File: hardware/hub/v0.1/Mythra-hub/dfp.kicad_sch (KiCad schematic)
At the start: 0 parts

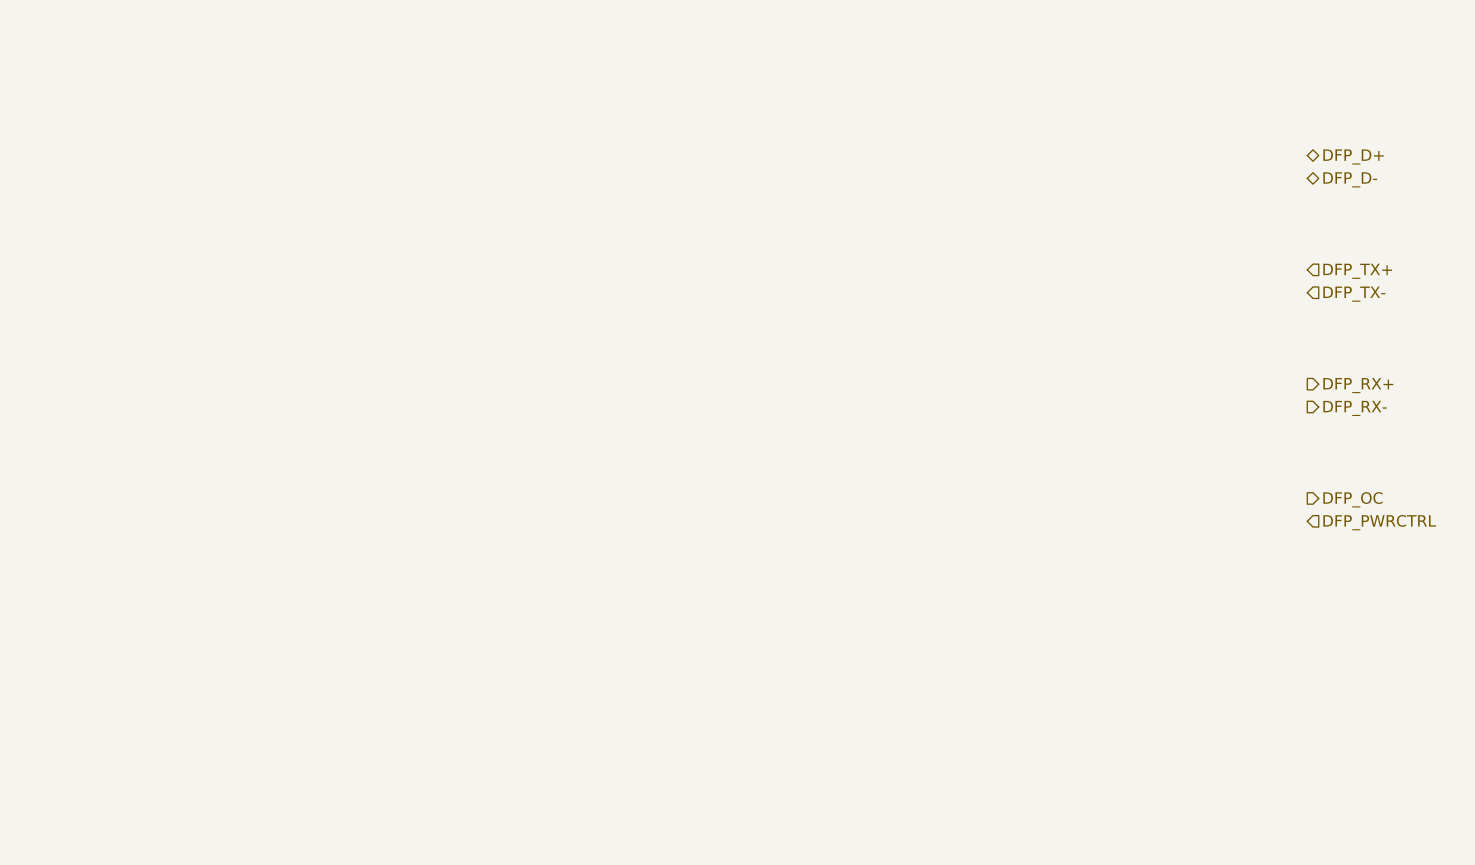
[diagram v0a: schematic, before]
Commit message: Created the DC-DC supply for the hub's core 1.1V rail and added the DFP Type-C recepticals and their shield components
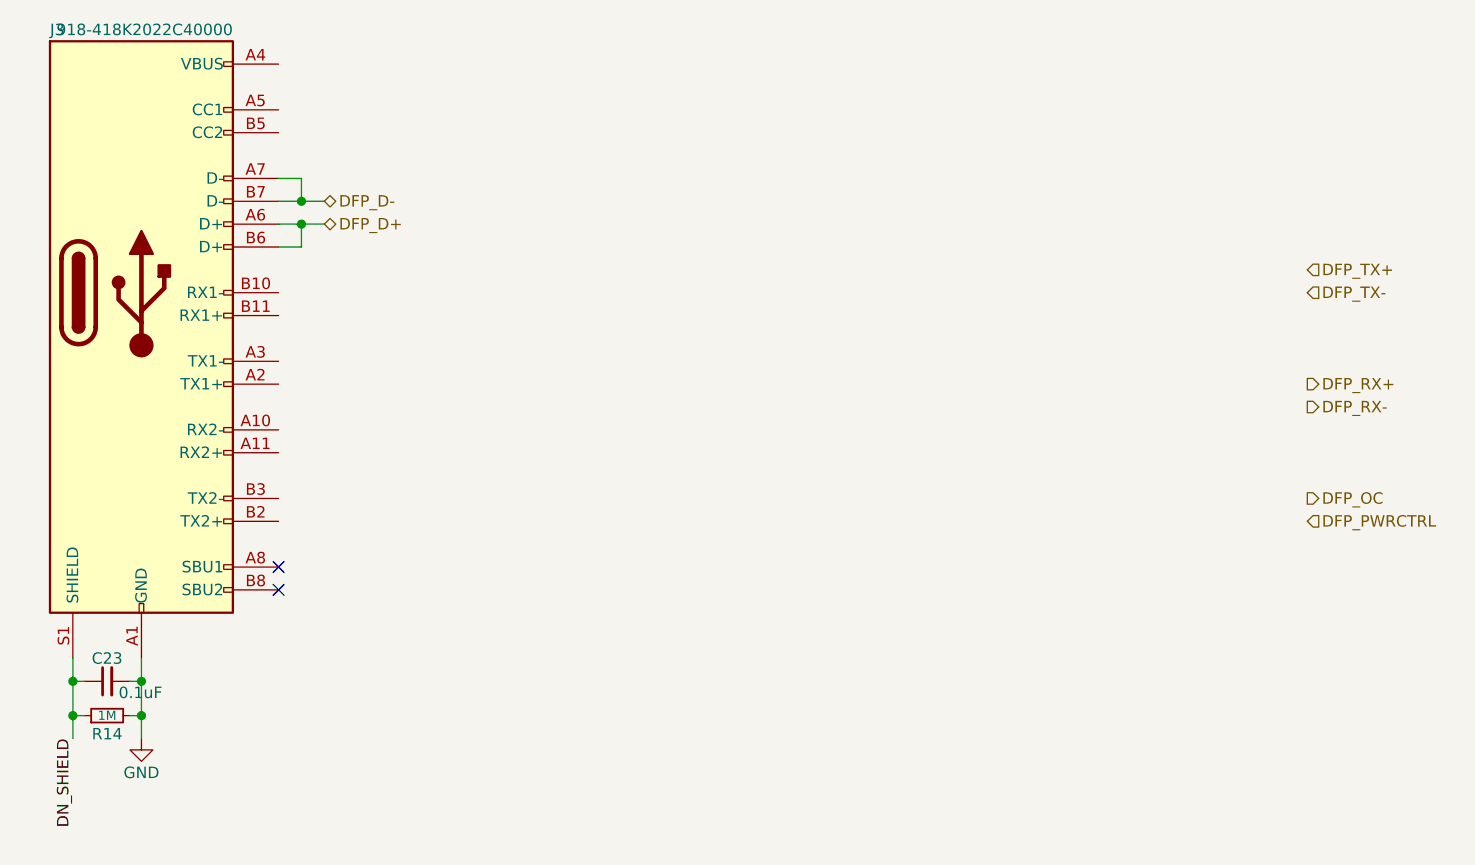
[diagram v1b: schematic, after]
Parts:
- added C23: 0.1uF, rhais_rcl:C0402, symbol Device:C_Small
- added J3: 918-418K2022C40000, rhais_usb:USB-3.1-Type-C_In-PCB, symbol Connector:USB_C_Receptacle
- added R14: 1M, rhais_rcl:R0402, symbol Device:R_Small
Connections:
- net DFP_D+: now also J3.A6 (D+), J3.B6 (D+)
- net DFP_D-: now also J3.A7 (D-), J3.B7 (D-)
- new net: J3.A4 (VBUS), J3.A9 (VBUS), J3.B4 (VBUS), J3.B9 (VBUS)
- new net DN_SHIELD: C23.1, J3.S1 (SHIELD), R14.1
- new net GND: C23.2, J3.A1 (GND), J3.A12 (GND), J3.B1 (GND), J3.B12 (GND), R14.2
- no-connect marks 0 -> 2
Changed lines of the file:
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@@
 (kicad_sch (version 20210621) (generator eeschema)
   (paper "A4")
-  (hierarchical_label "DFP_D+" (shape bidirectional) (at 165.1 88.9 0)
-    (effects (font (size 1.27 1.27)) (justify left))
-  )
-  (hierarchical_label "DFP_D-" (shape bidirectional) (at 165.1 91.44 0)
+  (junction (at 27.94 147.32) (diameter 1.016) (color 0 0 0 0))
+  (junction (at 27.94 151.13) (diameter 1.016) (color 0 0 0 0))
+  (junction (at 35.56 147.32) (diameter 1.016) (color 0 0 0 0))
+  (junction (at 35.56 151.13) (diameter 1.016) (color 0 0 0 0))
+  (junction (at 53.34 93.98) (diameter 1.016) (color 0 0 0 0))
+  (junction (at 53.34 96.52) (diameter 1.016) (color 0 0 0 0))
+  (no_connect (at 50.8 134.62))
+  (no_connect (at 50.8 137.16))
+  (wire (pts (xy 27.94 147.32) (xy 27.94 144.78))
+    (stroke (width 0) (type solid) (color 0 0 0 0))
+  )
+  (wire (pts (xy 27.94 151.13) (xy 27.94 147.32))
+    (stroke (width 0) (type solid) (color 0 0 0 0))
+  )
+  (wire (pts (xy 27.94 151.13) (xy 27.94 153.67))
+    (stroke (width 0) (type solid) (color 0 0 0 0))
+  )
+  (wire (pts (xy 29.21 147.32) (xy 27.94 147.32))
+    (stroke (width 0) (type solid) (color 0 0 0 0))
+  )
+  (wire (pts (xy 29.21 151.13) (xy 27.94 151.13))
+    (stroke (width 0) (type solid) (color 0 0 0 0))
+  )
+  (wire (pts (xy 34.29 147.32) (xy 35.56 147.32))
+    (stroke (width 0) (type solid) (color 0 0 0 0))
+  )
+  (wire (pts (xy 34.29 151.13) (xy 35.56 151.13))
+    (stroke (width 0) (type solid) (color 0 0 0 0))
+  )
+  (wire (pts (xy 35.56 147.32) (xy 35.56 144.78))
+    (stroke (width 0) (type solid) (color 0 0 0 0))
+  )
+  (wire (pts (xy 35.56 151.13) (xy 35.56 147.32))
+    (stroke (width 0) (type solid) (color 0 0 0 0))
+  )
+  (wire (pts (xy 35.56 153.67) (xy 35.56 151.13))
+    (stroke (width 0) (type solid) (color 0 0 0 0))
+  )
+  (wire (pts (xy 50.8 93.98) (xy 53.34 93.98))
+    (stroke (width 0) (type solid) (color 0 0 0 0))
+  )
+  (wire (pts (xy 50.8 96.52) (xy 53.34 96.52))
+    (stroke (width 0) (type solid) (color 0 0 0 0))
+  )
+  (wire (pts (xy 53.34 91.44) (xy 50.8 91.44))
+    (stroke (width 0) (type solid) (color 0 0 0 0))
+  )
+  (wire (pts (xy 53.34 93.98) (xy 53.34 91.44))
+    (stroke (width 0) (type solid) (color 0 0 0 0))
+  )
+  (wire (pts (xy 53.34 96.52) (xy 53.34 99.06))
+    (stroke (width 0) (type solid) (color 0 0 0 0))
+  )
+  (wire (pts (xy 53.34 99.06) (xy 50.8 99.06))
+    (stroke (width 0) (type solid) (color 0 0 0 0))
+  )
+  (wire (pts (xy 55.88 93.98) (xy 53.34 93.98))
+    (stroke (width 0) (type solid) (color 0 0 0 0))
+  )
+  (wire (pts (xy 55.88 96.52) (xy 53.34 96.52))
+    (stroke (width 0) (type solid) (color 0 0 0 0))
+  )
+  (label "DN_SHIELD" (at 27.94 153.67 270)
+    (effects (font (size 1.27 1.27)) (justify right bottom))
+  )
+  (hierarchical_label "DFP_D-" (shape bidirectional) (at 55.88 93.98 0)
+    (effects (font (size 1.27 1.27)) (justify left))
+  )
+  (hierarchical_label "DFP_D+" (shape bidirectional) (at 55.88 96.52 0)
     (effects (font (size 1.27 1.27)) (justify left))
   )
@@
     (effects (font (size 1.27 1.27)) (justify left))
   )
+  (symbol (lib_id "power:GND") (at 35.56 153.67 0)
+    (in_bom yes) (on_board yes)
+    (property "Reference" "#PWR018" (id 0) (at 35.56 160.02 0)
+      (effects (font (size 1.27 1.27)) hide)
+    )
+    (property "Value" "GND" (id 1) (at 35.56 157.48 0))
+    (property "Footprint" "" (id 2) (at 35.56 153.67 0)
+      (effects (font (size 1.27 1.27)) hide)
+    )
+    (property "Datasheet" "" (id 3) (at 35.56 153.67 0)
+      (effects (font (size 1.27 1.27)) hide)
+    )
+    (pin "1")
+  )
+  (symbol (lib_id "Device:R_Small") (at 31.75 151.13 90)
+    (in_bom yes) (on_board yes)
+    (property "Reference" "R14" (id 0) (at 31.75 153.924 90)
+      (effects (font (size 1.27 1.27)) (justify top))
+    )
+    (property "Value" "1M" (id 1) (at 31.75 151.13 90)
+      (effects (font (size 1.016 1.016)))
+    )
+    (property "Footprint" "rhais_rcl:R0402" (id 2) (at 31.75 151.13 0)
+      (effects (font (size 1.27 1.27)) hide)
+    )
+    (property "Datasheet" "https://www.farnell.com/datasheets/2860681.pdf" (id 3) (at 31.75 151.13 0)
+      (effects (font (size 1.27 1.27)) hide)
+    )
+    (property "MFR" "Multicomp Pro" (id 4) (at 31.75 151.13 0)
+      (effects (font (size 1.27 1.27)) hide)
+    )
+    (property "MPN" "MCWR04X1004FTL" (id 5) (at 31.75 151.13 0)
+      (effects (font (size 1.27 1.27)) hide)
+    )
+    (property "OC_FARNELL" "2447127" (id 6) (at 31.75 151.13 0)
+      (effects (font (size 1.27 1.27)) hide)
+    )
+    (property "URL_FARNELL" "https://uk.farnell.com/multicomp/mcwr04x1004ftl/res-1m-1-0-0625w-0402-thick-film/dp/2447127" (id 7) (at 31.75 151.13 0)
+      (effects (font (size 1.27 1.27)) hide)
+    )
+    (pin "1")
+    (pin "2")
+  )
+  (symbol (lib_id "Device:C_Small") (at 31.75 147.32 90)
+    (in_bom yes) (on_board yes)
+    (property "Reference" "C23" (id 0) (at 31.75 144.78 90))
+    (property "Value" "0.1uF" (id 1) (at 33.02 148.59 90)
+      (effects (font (size 1.27 1.27)) (justify right))
+    )
+    (property "Footprint" "rhais_rcl:C0402" (id 2) (at 31.75 147.32 0)
+      (effects (font (size 1.27 1.27)) hide)
+    )
+    (property "Datasheet" "~" (id 3) (at 31.75 147.32 0)
+      (effects (font (size 1.27 1.27)) hide)
+    )
+    (pin "1")
+    (pin "2")
+  )
+  (symbol (lib_id "Connector:USB_C_Receptacle") (at 35.56 104.14 0)
+    (in_bom yes) (on_board yes)
+    (property "Reference" "J3" (id 0) (at 25.4 74.93 0)
+      (effects (font (size 1.27 1.27)) (justify left))
+    )
+    (property "Value" "918-418K2022C40000" (id 1) (at 45.72 74.93 0)
+      (effects (font (size 1.27 1.27)) (justify right))
+    )
+    (property "Footprint" "rhais_usb:USB-3.1-Type-C_In-PCB" (id 2) (at 39.37 104.14 0)
+      (effects (font (size 1.27 1.27)) hide)
+    )
+    (property "Datasheet" "https://datasheet.lcsc.com/lcsc/2103051833_Jing-Extension-of-the-Electronic-Co.-918-418K2022C40000_C168700.pdf" (id 3) (at 39.37 104.14 0)
+      (effects (font (size 1.27 1.27)) hide)
+    )
+    (property "MFR" "Jing ext of Electronic Co." (id 4) (at 35.56 104.14 0)
+      (effects (font (size 1.27 1.27)) hide)
+    )
+    (property "MPN" "918-418K2022C40000" (id 5) (at 35.56 104.14 0)
+      (effects (font (size 1.27 1.27)) hide)
+    )
+    (property "OC_LCSC" "C168700" (id 6) (at 35.56 104.14 0)
+      (effects (font (size 1.27 1.27)) hide)
+    )
+    (property "URL_LCSC" "https://lcsc.com/product-detail/USB-Connectors_Jing-Extension-of-the-Electronic-Co-918-418K2022C40000_C168700.html" (id 7) (at 35.56 104.14 0)
+      (effects (font (size 1.27 1.27)) hide)
+    )
+    (pin "A1")
+    (pin "A10")
+    (pin "A11")
+    (pin "A12")
+    (pin "A2")
+    (pin "A3")
+    (pin "A4")
+    (pin "A5")
+    (pin "A6")
+    (pin "A7")
+    (pin "A8")
+    (pin "A9")
+    (pin "B1")
+    (pin "B10")
+    (pin "B11")
+    (pin "B12")
+    (pin "B2")
+    (pin "B3")
+    (pin "B4")
+    (pin "B5")
+    (pin "B6")
+    (pin "B7")
+    (pin "B8")
+    (pin "B9")
+    (pin "S1")
+  )
 )
